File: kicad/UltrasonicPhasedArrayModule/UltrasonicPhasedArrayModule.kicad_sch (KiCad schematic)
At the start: 12 parts, among them J1 Conn_02x08_Top_Bottom, Q1 2N2222, Q2 2N2222, Q3 2N2222, Q4 2N2222, U1 74HC138, U2 74HC04

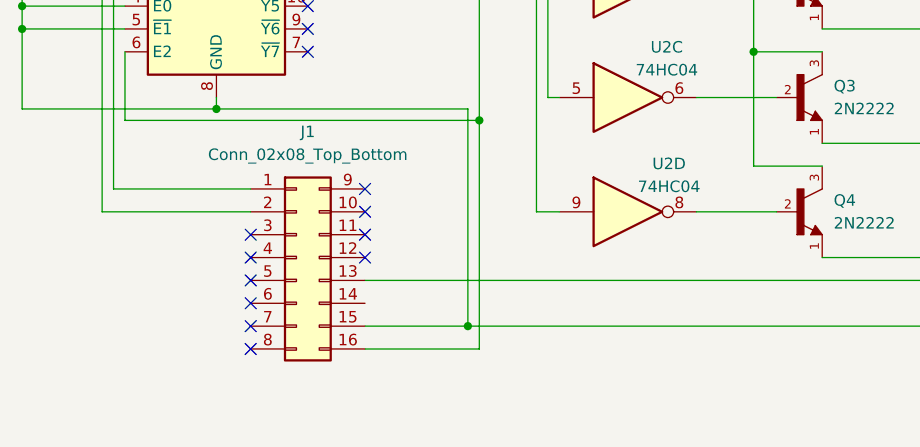
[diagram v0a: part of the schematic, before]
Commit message: Updated some of the KiCAD files and started on UPA sensor module code.
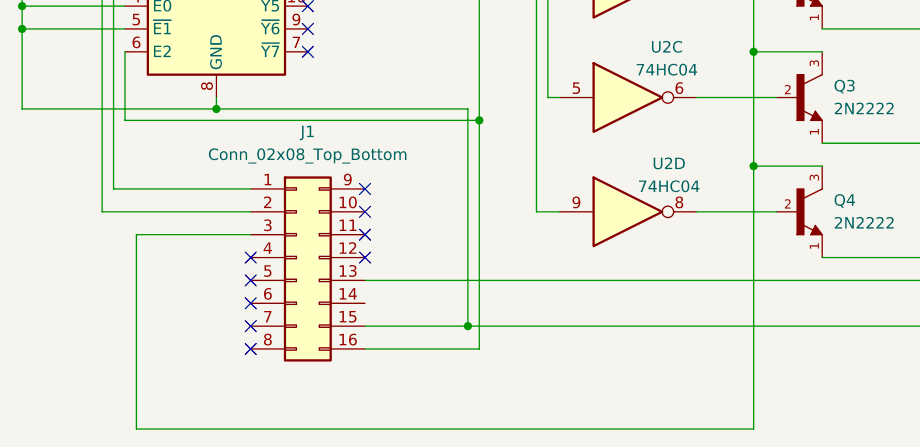
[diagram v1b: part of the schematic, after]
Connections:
- net at J1.3 (Pin_3): now also Q1.3, Q2.3, Q3.3, Q4.3
- no-connect marks 14 -> 13
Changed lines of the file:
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@@
+	)
+	(junction
+		(at 157.48 109.22)
+		(diameter 0)
+		(color 0 0 0 0)
 	)
 	(junction
@@
 	)
 	(no_connect
-		(at 101.6 116.84)
-	)
-	(no_connect
 		(at 114.3 114.3)
 	)
@@
 	(wire
 		(pts
+			(xy 88.9 116.84) (xy 88.9 138.43)
+		)
+		(stroke
+			(width 0)
+			(type default)
+		)
+	)
+	(wire
+		(pts
 			(xy 185.42 121.92) (xy 114.3 121.92)
 		)
@@
 	(wire
 		(pts
+			(xy 157.48 138.43) (xy 157.48 109.22)
+		)
+		(stroke
+			(width 0)
+			(type default)
+		)
+	)
+	(wire
+		(pts
 			(xy 190.5 96.52) (xy 190.5 83.82)
 		)
@@
 	(wire
 		(pts
+			(xy 88.9 138.43) (xy 157.48 138.43)
+		)
+		(stroke
+			(width 0)
+			(type default)
+		)
+	)
+	(wire
+		(pts
 			(xy 107.95 81.28) (xy 135.89 81.28)
 		)
@@
 		)
 		(stroke
+			(width 0)
+			(type default)
+		)
+	)
+	(wire
+		(pts
+			(xy 101.6 116.84) (xy 88.9 116.84)
+		)
+		(stroke

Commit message: Pushing slight updates and progress on UPA
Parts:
- J1: footprint (none) -> Connector_IDC:IDC-Header_2x08_P2.54mm_Vertical
- LS1, LS2, LS3, LS4, MK1: footprint (none) -> UltrasonicTransducerReceiver:Ultrasonic Transducer-Receiver
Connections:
- no-connect marks 13 -> 14
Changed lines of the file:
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@@
+	)
+	(no_connect
+		(at 114.3 124.46)
 	)
 	(no_connect
@@
 			)
 		)
-		(property "Footprint" ""
+		(property "Footprint" "Connector_IDC:IDC-Header_2x08_P2.54mm_Vertical"
 			(at 106.68 119.38 0)
 			(effects
@@
 			)
 		)
-		(property "Footprint" ""
+		(property "Footprint" "UltrasonicTransducerReceiver:Ultrasonic Transducer-Receiver"
 			(at 207.391 107.95 0)
 			(effects
@@
 			)
 		)
-		(property "Footprint" ""
+		(property "Footprint" "UltrasonicTransducerReceiver:Ultrasonic Transducer-Receiver"
 			(at 207.391 120.65 0)
 			(effects
@@
 			)
 		)
-		(property "Footprint" ""
+		(property "Footprint" "UltrasonicTransducerReceiver:Ultrasonic Transducer-Receiver"
 			(at 191.77 72.898 90)
 			(effects
@@
 			)
 		)
-		(property "Footprint" ""
+		(property "Footprint" "UltrasonicTransducerReceiver:Ultrasonic Transducer-Receiver"
 			(at 207.391 82.55 0)
 			(effects
@@
 			)
 		)
-		(property "Footprint" ""
+		(property "Footprint" "UltrasonicTransducerReceiver:Ultrasonic Transducer-Receiver"
 			(at 207.391 95.25 0)
 			(effects

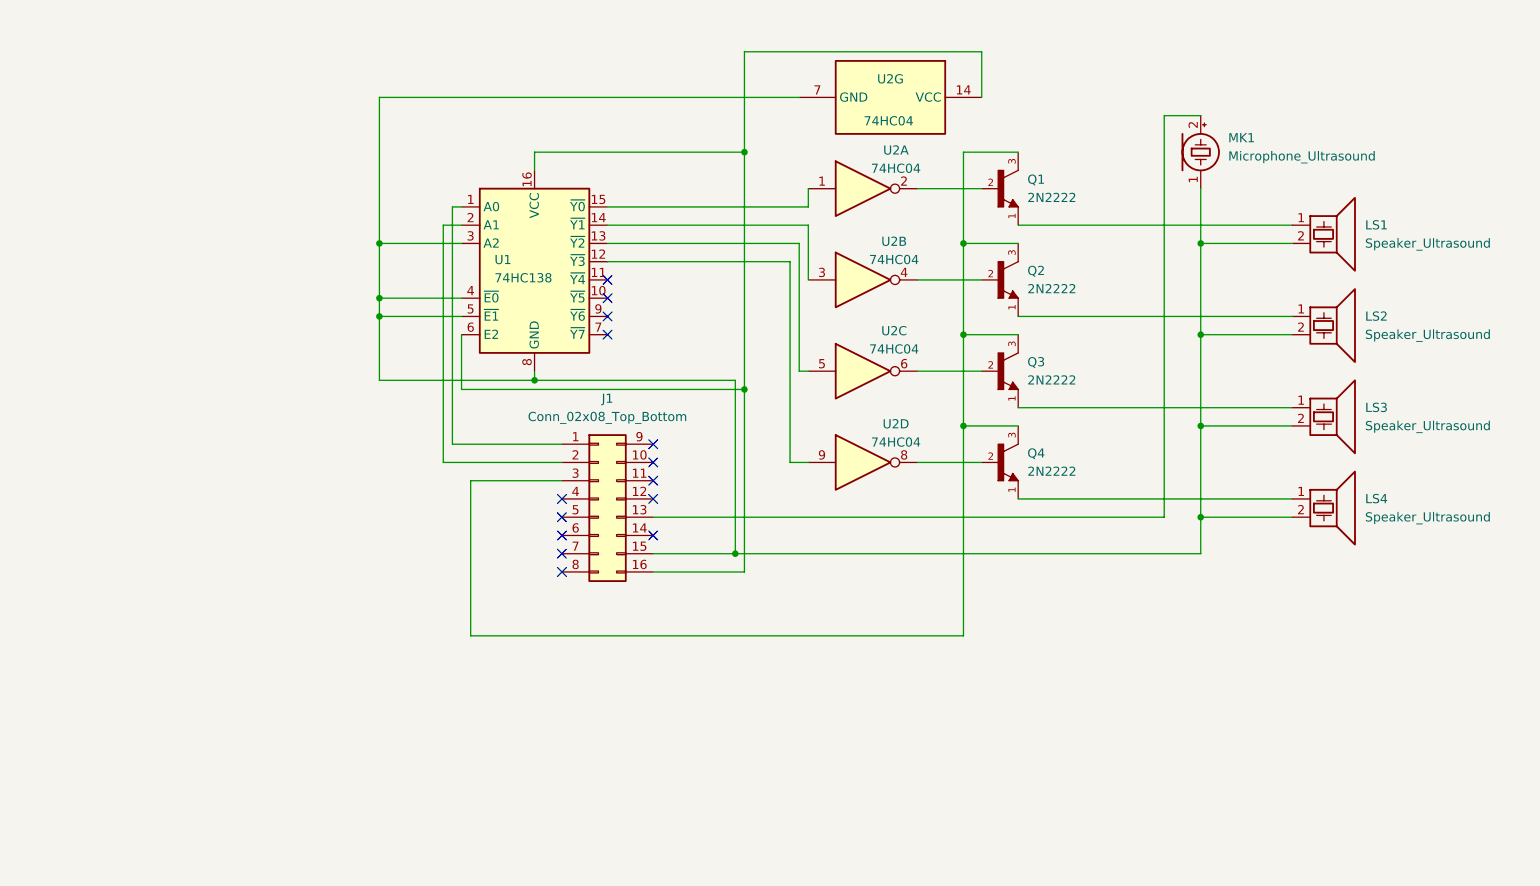
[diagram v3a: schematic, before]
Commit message: Started work on UPA OP-AMP Circuit
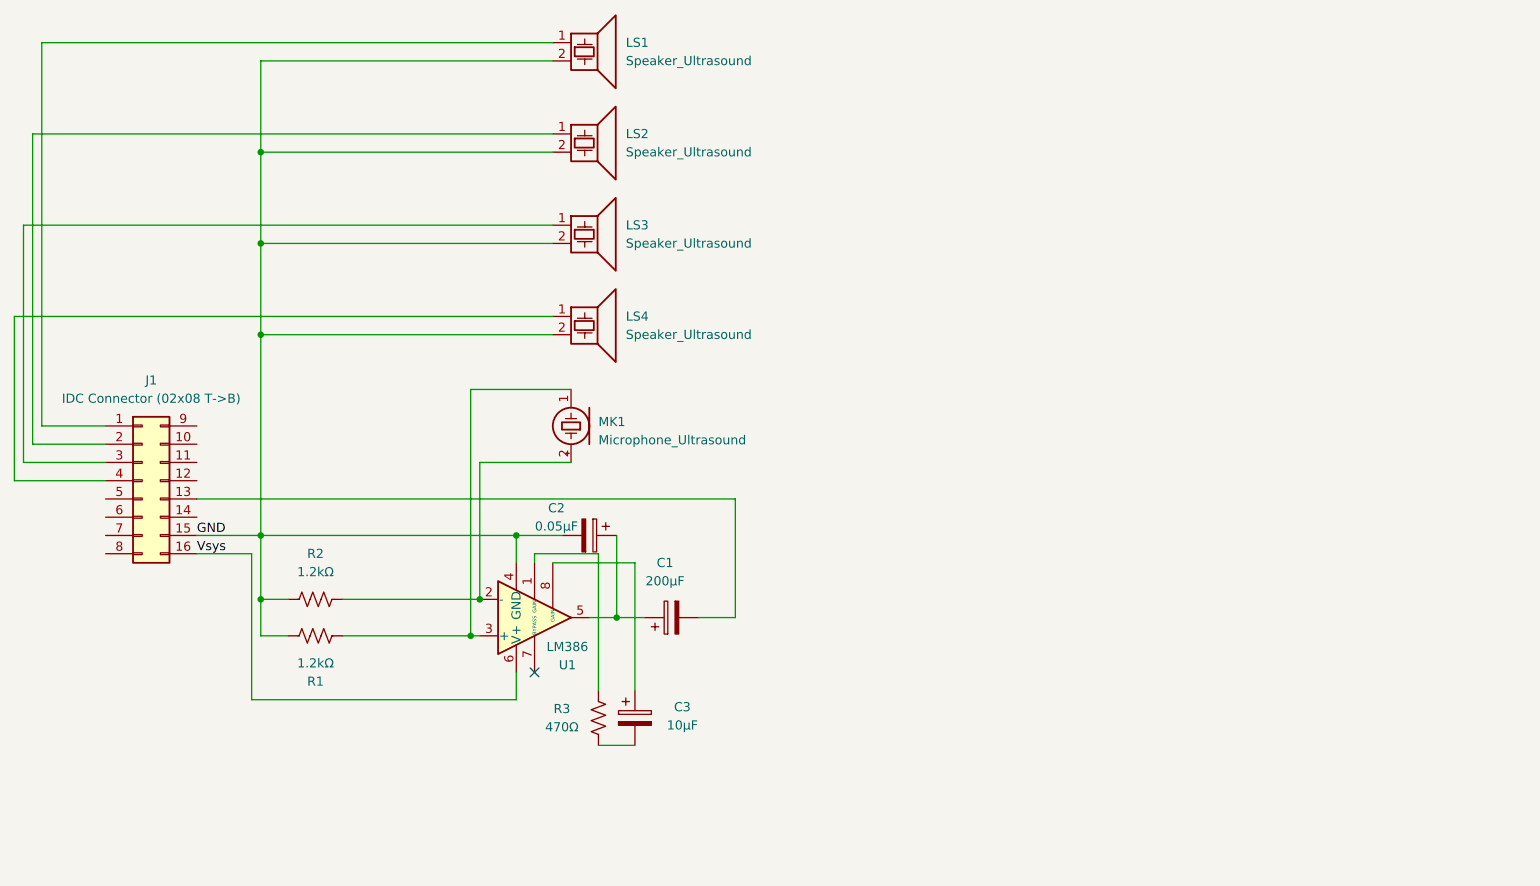
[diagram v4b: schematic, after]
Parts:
- removed Q1, Q2, Q3, Q4: 2N2222, 2N2222:TO127P584H533-3, symbol 2N2222:2N2222
- removed U1: 74HC138, Package_DIP:DIP-16_W7.62mm, symbol 74xx:74HC138
- removed U2: 74HC04, Package_DIP:DIP-14_W7.62mm, symbol 74xx:74HC04
- added C1: 200μF, symbol Device:C_Polarized
- added C2: 0.05μF, symbol Device:C_Polarized
- added C3: 10μF, symbol Device:C_Polarized
- added R1, R2: 1.2kΩ, symbol Device:R_US
- added R3: 470Ω, symbol Device:R_US
- added U1: LM386, Package_DIP:DIP-8_W7.62mm, symbol Amplifier_Audio:LM386
- J1: value Conn_02x08_Top_Bottom -> IDC Connector (02x08 T->B)
- LS1, LS2, LS3, LS4, MK1: footprint UltrasonicTransducerReceiver:Ultrasonic Transducer-Receiver -> (none)
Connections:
- net at J1.1 (Pin_1): now also LS1.1
- net Vsys: now reaches J1.16 (Pin_16)
- net Vsys: now also U1.6 (V+)
- net at J1.2 (Pin_2): now also LS2.1
- net GND: now reaches J1.15 (Pin_15), LS1.2, LS2.2, LS3.2, LS4.2
- net GND: now also C2.2, R1.2, R2.1, U1.4 (GND); no longer MK1.1 (-)
- net at J1.13 (Pin_13): now also C1.2; no longer MK1.2 (+)
- net at J1.3 (Pin_3): now also LS3.1
- net at J1.4 (Pin_4): now also LS4.1
- new net: C3.1, U1.8 (GAIN)
- new net: C3.2, R3.1
- new net: R3.2, U1.1 (GAIN)
- new net: MK1.2 (+), R2.2, U1.2 (-)
- new net: MK1.1 (-), R1.1, U1.3 (+)
- new net: C1.1, C2.1, U1.5
- no-connect marks 14 -> 1

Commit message: Added missing 10oh resistor on output of LM386
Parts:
- added R4: 10Ω, symbol Device:R_US
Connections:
- net GND: now also R4.1; no longer C2.2, U1.4 (GND)
- new net: C2.2, R4.2, U1.4 (GND)
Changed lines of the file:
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@@
+	(wire
+		(pts
+			(xy 77.47 124.46) (xy 59.69 124.46)
+		)
+		(stroke
+			(width 0)
+			(type default)
+		)
+	)
 	(wire
 		(pts
@@
 	(wire
 		(pts
-			(xy 95.25 124.46) (xy 59.69 124.46)
+			(xy 95.25 124.46) (xy 85.09 124.46)
 		)
 		(stroke
@@
 		)
 	)
+	(symbol
+		(lib_id "Device:R_US")
+		(at 81.28 124.46 90)
+		(unit 1)
+		(exclude_from_sim no)
+		(in_bom yes)
+		(on_board yes)
+		(dnp no)
+		(property "Reference" "R4"
+			(at 81.28 126.746 90)
+			(effects
+				(font
+					(size 1.27 1.27)
+				)
+			)
+		)
+		(property "Value" "10Ω"
+			(at 81.28 129.286 90)
+			(effects
+				(font
+					(size 1.27 1.27)
+				)
+			)
+		)
+		(property "Footprint" ""
+			(at 81.534 123.444 90)
+			(effects
+				(font
+					(size 1.27 1.27)
+				)
+				(hide yes)
+			)
+		)
+		(property "Datasheet" "~"
+			(at 81.28 124.46 0)
+			(effects
+				(font
+					(size 1.27 1.27)
+				)
+				(hide yes)
+			)
+		)
+		(property "Description" "Resistor, US symbol"
+			(at 81.28 124.46 0)
+			(effects
+				(font
+					(size 1.27 1.27)
+				)
+				(hide yes)
+			)
+		)
+		(pin "2"
+		)
+		(pin "1"
+		)
+		(instances
+			(project "UltrasonicPhasedArrayModule"
+				(path "/6750e596-42dc-499b-95fe-076f8cb851f4"
+					(reference "R4")
+					(unit 1)
+				)
+			)
+		)
+	)

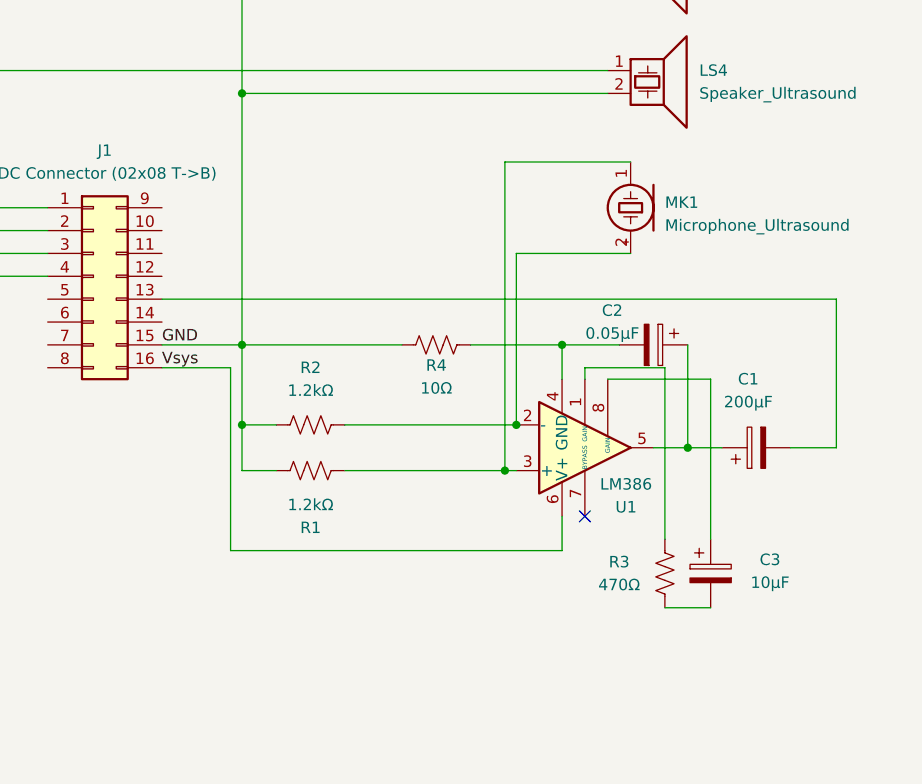
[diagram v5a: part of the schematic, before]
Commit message: KiCAD Files Completed and General UPA Update
KiCAD design files for the base module and UPA module are completed and on order.

The UPA sensor code is now fully operational. One issue: accuracy of the beam forming. A recalculation of delay timing is required. EEPROM does not seem to write/read properly on breadboard, though this could be to faulty connections. Further testing is required.

KNOWN ISSUES:
* UPA beam forming not accurate
* EEPROM fails to read/write properly.
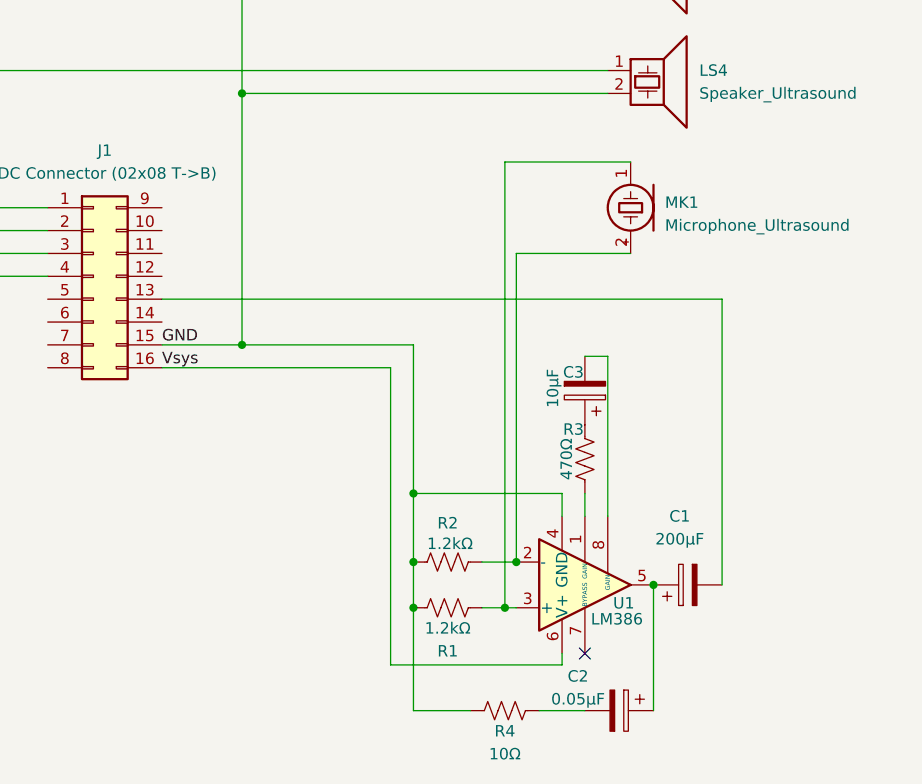
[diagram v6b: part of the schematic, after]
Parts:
- C1: footprint (none) -> Capacitor_THT:CP_Radial_Tantal_D8.0mm_P2.50mm
- C2: footprint (none) -> Capacitor_THT:C_Disc_D3.0mm_W1.6mm_P2.50mm
- C3: footprint (none) -> Capacitor_THT:CP_Radial_Tantal_D5.0mm_P2.50mm
- LS1, LS2, LS3, LS4, MK1: footprint (none) -> UltrasonicTransducerReceiver:Ultrasonic Transducer-Receiver
- R1, R2, R3, R4: footprint (none) -> Resistor_THT:R_Axial_DIN0207_L6.3mm_D2.5mm_P10.16mm_Horizontal
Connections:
- net GND: now also U1.4 (GND)
- net at C2.2, R4.2: no longer U1.4 (GND)
- net at C3.1: now also R3.1; no longer U1.8 (GAIN)
- net at C3.2: now also U1.8 (GAIN); no longer R3.1
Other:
- moved on the sheet: C1, C2, C3, R1, R2, R3, R4, U1
